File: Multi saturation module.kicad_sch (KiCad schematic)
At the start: 38 parts, among them J1 AudioJack2, J3 AudioJack2, U1 NE5532, U2 NE5532, U3 NE5532

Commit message: renamed the project
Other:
- title: Eurorack Transformer Saturation Module -> Eurorack Multi Saturation Module

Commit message: revision 0.4
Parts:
- removed C?: 1uF, symbol Device:C
- removed C?: 470uF, symbol Device:C_Polarized
- removed D?: 4148, symbol Device:D
- removed Q?: NPN, symbol Simulation_SPICE:NPN
- removed R?: 10k, symbol Device:R
- removed R? (x2): 1k5, symbol Device:R
- removed U?: VTL5C, OptoDevice:PerkinElmer_VTL5C, symbol Isolator:VTL5C
- added C1: 1uF, symbol Device:C
- added C3: 0.1uF, symbol Device:C
- added D2, D3: LED, symbol Device:LED
- added D4, D5: 4148, symbol Device:D
- added R1, R2: 10R, symbol Device:R
- added R11: 100k, symbol Device:R
- added R14, R21, R5, R9: 10k, symbol Device:R
- added R22: 6.8k, symbol Device:R
- added R3: 680R, symbol Device:R
- added R6: 330R, symbol Device:R
- added RV3: Dry_gain_10k, symbol Device:R_Potentiometer_Trim
- added SW2: Bypass_sw_DPDT, symbol Switch:SW_DPDT_x2
- added SW3: SW_SPST, symbol Switch:SW_SPST
- added U1: NE5532, symbol Amplifier_Operational:NE5532
- added U3: VTL5C, OptoDevice:PerkinElmer_VTL5C, symbol Isolator:VTL5C
- added unit 3 of U5
- RV2: renamed from RV3; value 10k -> Wet_gain_10k
- renumbered C1 to C2, R12 to R10, R9 to R13, R2 to R7, U3 to U4, U1 to U5
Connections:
- net Mix is gone; now on net Audio_out: R?.1, U?.3
- net +12V: now also U5.8 (V+)
- net -12V: now also U5.4 (V-)
- net Audio_out: no longer U?.7
- net Dry: now also U?.5 (+); no longer U2.5 (+)
- net GND: now also D4.2 (A), D5.1 (K), R11.2, R22.2, R6.2, R9.1, RV3.1, RV3.2, U3.4; no longer U?.5 (+)
- net Wet: now also C3.1, R11.1; no longer C2.1, R10.1
- net at U?.6 (-): now also R14.2, RV3.3
- net Clipping_diodes: now reaches R13.1, U4.1, U?.4
- net Clipping_diodes: now also SW3.2 (B)
- new net: C1.2, R1.1
- new net: R1.2, U1.5 (+)
- new net: R14.1, R?.2, U?.7
- new net: R2.1, U1.3 (+)
- new net: R2.2, R5.1, SW2.1 (A)
- new net: R5.2, R9.2, SW2.4 (A), U3.3
- new net: R6.1, U1.6 (-), U3.1 (-)
- new net: D2.1 (K), D3.2 (A), SW3.1 (A)
- new net: C1.1, U1.1, U1.2 (-)
- new net: C3.2, SW2.5 (B)
- new net: R21.2, SW2.2 (B), U2.7
- new net: SW2.3 (C), SW2.6 (C)
- new net: D2.2 (A), D3.1 (K), D4.1 (K), D5.2 (A)
- new net: R3.2, U1.7
- new net: R21.1, R22.1, U2.6 (-)
- new net: R3.1, U3.2 (+)
- new net: C2.1, R10.1, U2.5 (+)
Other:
- note added: "VTL5C3 R17 = 47k Silonex 32SR3 R17 = 470R Handmade Vactrol with 5mm led and LDR R17 = 47k"
- note added: "Vactrol Saturation Stage"
- note added: "dry gain compensation"
- note removed: "Output gain stage"
- note removed: "VTL5C3 R13 = 47k Silonex 32SR3 R12 = 470R Handmade Vactrol with 5mm led and LDR = 47k"
- moved on the sheet: C2, D?, J1, J?, R10, R13, R7, R?, RV2, RV?, SW?A, SW?B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

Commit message: revision 0.4 update
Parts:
- removed R9: 10k, symbol Device:R
- added C4, C5: 22uF, symbol Device:C_Polarized
- added D1: LED, symbol Device:LED
- added D7, D8: 4001, symbol Device:D
- added J4, J5: Dry_audio_out, symbol Connector_Audio:AudioJack2
- J1: value AudioJack2 -> Audio_in
- J3: value AudioJack2 -> Mix_audio_out
- renumbered C2 to C1, C1 to C2, D4 to D5, D5 to D6, R6 to R10, R5 to R12, R13 to R14, R14 to R15, R7 to R2, R2 to R4, R1 to R5, R10 to R6, R3 to R7, R21 to R8, R22 to R9, U2 to U1, U1 to U2
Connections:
- net +12V: now also C4.1, D7.1 (K)
- net -12V: now also C5.2, D8.2 (A)
- net Dry: now also J4.T
- net GND: now also C4.2, C5.1, J4.S, J5.S
- net Wet: now also J5.T
- net at R4.1: now also R12.2, SW2.1 (A); no longer U2.3 (+)
- net at SW2.4 (A), U3.3: now also R12.1; no longer R12.2
- net at R10.1, U2.6 (-), U3.1 (-): now also D1.1 (K)
- net Mix_CV_in: now reaches J?.T, R?.1, RV?.3
- net at R7.1, U3.2 (+): now also D1.2 (A)
- net Audio_out renamed Mix_audio_out
- new net: R4.2, U2.3 (+)
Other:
- moved on the sheet: C1, C2, C3, D2, D3, D5, D6, D?, J1, J3, J?, R10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

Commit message: rev 0.5 update
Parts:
- added J6: EURO_PWR_2x5, DIYSynthMNL:IDC-Header_2x05_P2.54mm_Vertical_BigPads, symbol eurocad:EURO_PWR_2x5
- added R22: 330R, DIYSynthMNL:R_quarter_watt_L6.3mm_D2.5mm_P7.62mm, symbol Device:R
- C1, C3: footprint (none) -> DIYSynthMNL:C_Rect_L7.0mm_W2.0mm_P5.00mm_BigPads
- C2: footprint (none) -> DIYSynthMNL:C_Rect_L7.0mm_W4.5mm_P5.00mm_BigPads
- C4, C5: footprint (none) -> DIYSynthMNL:CP_Radial_D4.0mm_P1.50mm
- D1, D2, D3, D?: footprint (none) -> DIYSynthMNL:LED_D5.0mm_BigPads
- D5, D6: footprint (none) -> DIYSynthMNL:D_4148_BigPads
- D7, D8: footprint (none) -> DIYSynthMNL:D_DO-41_SOD81_P7.62mm_Horizontal
- J1, J3, J4, J?: footprint (none) -> DIYSynthMNL:AudioJack_3.5mm_long_pads; symbol Connector_Audio:AudioJack2 -> benjiaomodular:PJ3001F
- J5: value Dry_audio_out -> Wet_audio_out; footprint (none) -> DIYSynthMNL:AudioJack_3.5mm_long_pads; symbol Connector_Audio:AudioJack2 -> benjiaomodular:PJ3001F
- R10, R11, R12, R14, R15, R4, R5, R6, R7, R8, R9, R? (x9): footprint (none) -> DIYSynthMNL:R_quarter_watt_L6.3mm_D2.5mm_P7.62mm
- R2: value 10k -> 100k; footprint (none) -> DIYSynthMNL:R_quarter_watt_L6.3mm_D2.5mm_P7.62mm
- RV2, RV3: footprint (none) -> DIYSynthMNL:Potentiometer_Bourns_3296W_Vertical_BigPads
- RV? (x2): footprint (none) -> DIYSynthMNL:Potentiometer_RV09_BigPads
- SW2, SW? (x2): footprint (none) -> benjiaomodular:ToggleSwitch_MTS-202_DPDT
- SW3: footprint (none) -> benjiaomodular:ToggleSwitch_MTS-102_SPDT
- T?: footprint (none) -> RF_Mini-Circuits:Mini-Circuits_CD636_H4.11mm; symbol Device:Transformer_1P_1S -> Transformer:ADTT3-2
- U1, U2, U4, U5, U? (x3): footprint (none) -> DIYSynthMNL:DIP-8_W7.62mm_LongPads
- U3, U?: footprint OptoDevice:PerkinElmer_VTL5C -> DIYSynthMNL:Handmade_vactrol_5mm
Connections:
- net Clipping_diodes: now also R22.2; no longer SW3.2 (B)
- net GND: now also T?.1, J6.3 (GND), J6.4 (GND), J6.5 (GND), J6.6 (GND), J6.7 (GND), J6.8 (GND); no longer T?.2 (AB)
- net at D8.1 (K): now also J6.10 (-12V), J6.9 (-12V)
- net at R?.2: now also T?.3; no longer T?.1 (AA)
- net at R?.2, SW?.4 (A): now also T?.6; no longer T?.3 (SA)
- net at D7.2 (A): now also J6.1 (+12V), J6.2 (+12V)
- new net: R22.1, SW3.2 (B)
- no-connect marks 0 -> 7
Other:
- moved on the sheet: R2

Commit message: Revision 5 update
This commit is before I separate the schematic parts into boards.
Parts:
- added J7: EuroPower_JST_3P, DIYSynthMNL:Eurorack_power_jst_3P, symbol DIYSynthMNL:JST_Eurorack_power_3P
- D7, D8: footprint DIYSynthMNL:D_DO-41_SOD81_P7.62mm_Horizontal -> DIYSynthMNL:D_DO-41_SOD81_P7.62mm_Horizontal_BigPads
- SW3: symbol Switch:SW_SPST -> Switch:SW_SPDT
- T?: footprint RF_Mini-Circuits:Mini-Circuits_CD636_H4.11mm -> DIYSynthMNL:Audio_transformer_TL016-R
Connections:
- net GND: now also J7.2 (GND)
- net at D7.2 (A), J6.1 (+12V), J6.2 (+12V): now also J7.1 (+12v)
- net at D8.1 (K), J6.10 (-12V), J6.9 (-12V): now also J7.3 (-12v)
- net at D2.1 (K), D3.2 (A): now also SW3.2 (B); no longer SW3.1 (A)
- net at R22.1: now also SW3.1 (A); no longer SW3.2 (B)
- no-connect marks 7 -> 8
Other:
- moved on the sheet: C4, C5, D7, D8, J6, U2C, U4C, U5C, U?C

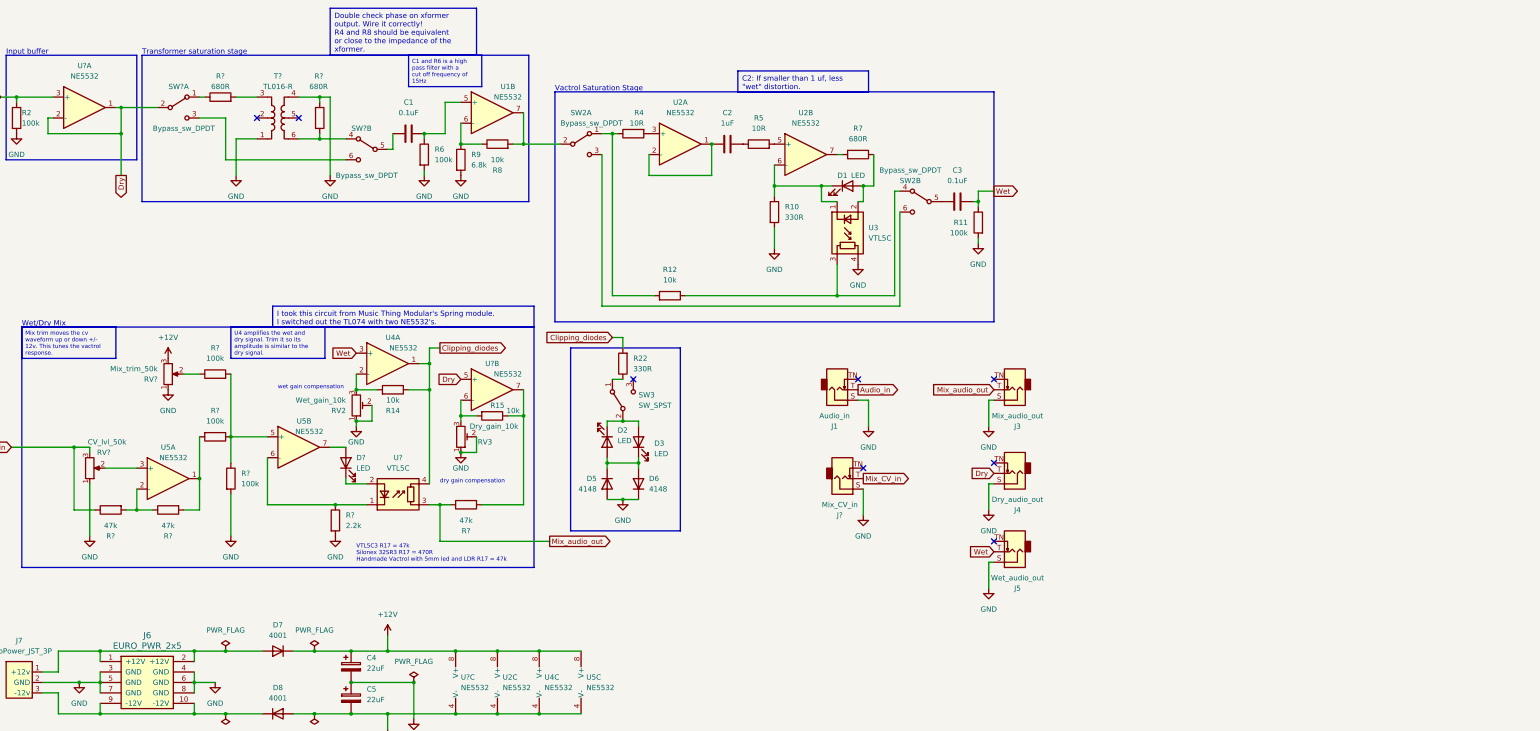
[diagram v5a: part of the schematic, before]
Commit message: Separate boards branch started
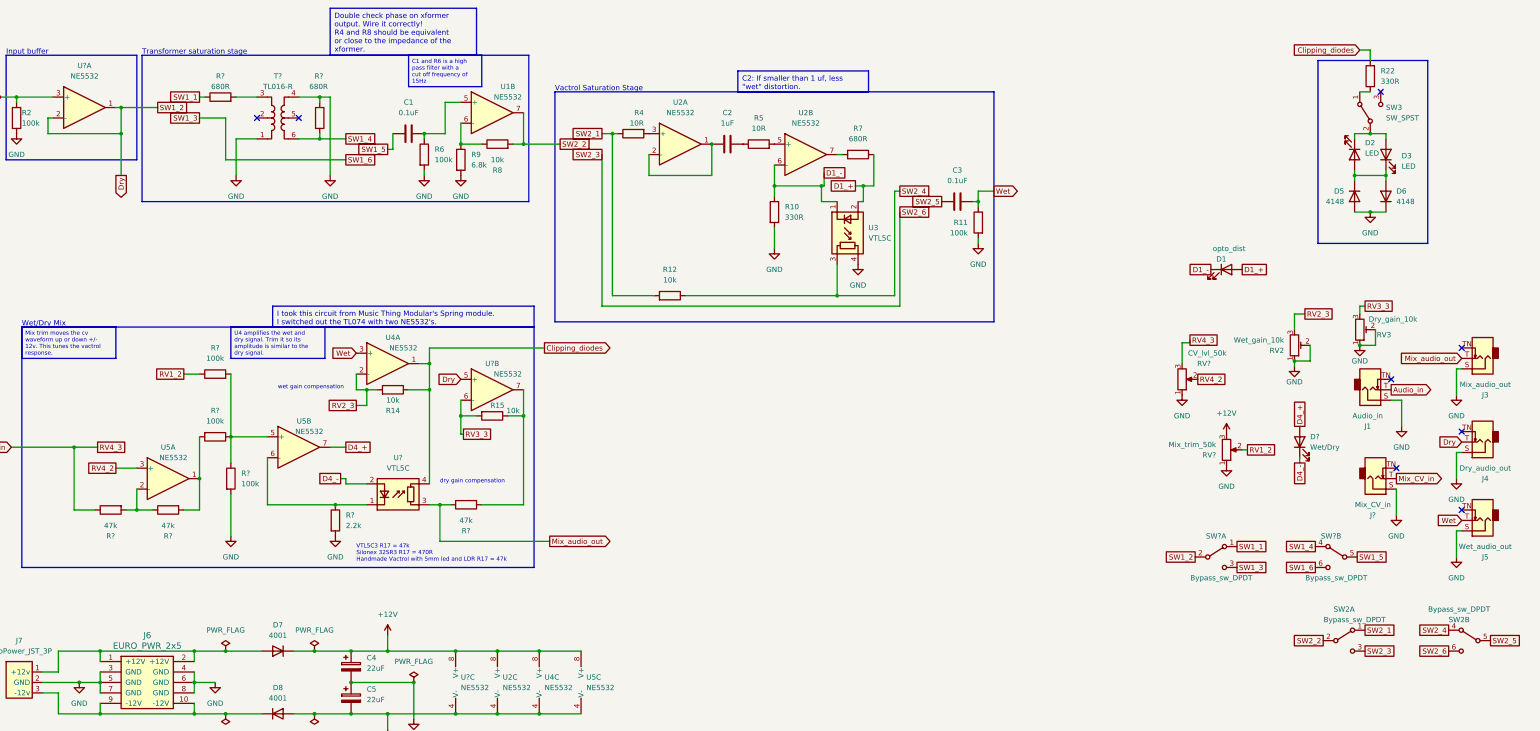
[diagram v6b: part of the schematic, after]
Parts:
- D1: value LED -> opto_dist
- D?: value LED -> Wet/Dry
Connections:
- net RV2_3: now reaches R14.2, RV2.3, U4.2 (-)
- net RV3_3: now reaches R15.2, RV3.3, U?.6 (-)
- net SW2_1: now reaches R12.2, R4.1, SW2.1 (A)
- net D4_+: now reaches D?.2 (A), U5.7
- net RV4_2: now reaches RV?.2, U5.3 (+)
- net D1_-: now reaches D1.1 (K), R10.1, U2.6 (-), U3.1 (-)
- net SW1_4: now reaches R?.2, SW?.4 (A), T?.6
- net D4_-: now reaches D?.1 (K), U?.2 (+)
- net SW2_5: now reaches C3.2, SW2.5 (B)
- net RV1_2: now reaches R?.1, RV?.2
- net SW2_2: now reaches R8.2, SW2.2 (B), U1.7
- net SW2_3: now reaches SW2.3 (C), SW2.6 (C)
- net SW2_4: now reaches R12.1, SW2.4 (A), U3.3
- net SW1_5: now reaches C1.2, SW?.5 (B)
- net SW1_3: now reaches SW?.3 (C), SW?.6 (C)
- net SW1_1: now reaches R?.1, SW?.1 (A)
- net D1_+: now reaches D1.2 (A), R7.1, U3.2 (+)
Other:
- moved on the sheet: D1, D2, D3, D5, D6, D?, J1, J3, J4, J5, J?, R22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

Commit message: Laid out footprints on three boards
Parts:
- removed C1, C3: 0.1uF, DIYSynthMNL:C_Rect_L7.0mm_W2.0mm_P5.00mm_BigPads, symbol Device:C
- removed C2: 1uF, DIYSynthMNL:C_Rect_L7.0mm_W4.5mm_P5.00mm_BigPads, symbol Device:C
- removed C4, C5: 22uF, DIYSynthMNL:CP_Radial_D4.0mm_P1.50mm, symbol Device:C_Polarized
- removed D1: opto_dist, DIYSynthMNL:LED_D5.0mm_BigPads, symbol Device:LED
- removed D2, D3: LED, DIYSynthMNL:LED_D5.0mm_BigPads, symbol Device:LED
- removed D5, D6: 4148, DIYSynthMNL:D_4148_BigPads, symbol Device:D
- removed D7, D8: 4001, DIYSynthMNL:D_DO-41_SOD81_P7.62mm_Horizontal_BigPads, symbol Device:D
- removed D?: Wet/Dry, DIYSynthMNL:LED_D5.0mm_BigPads, symbol Device:LED
- removed J1: Audio_in, DIYSynthMNL:AudioJack_3.5mm_long_pads, symbol benjiaomodular:PJ3001F
- removed J3: Mix_audio_out, DIYSynthMNL:AudioJack_3.5mm_long_pads, symbol benjiaomodular:PJ3001F
- removed J4: Dry_audio_out, DIYSynthMNL:AudioJack_3.5mm_long_pads, symbol benjiaomodular:PJ3001F
- removed J5: Wet_audio_out, DIYSynthMNL:AudioJack_3.5mm_long_pads, symbol benjiaomodular:PJ3001F
- removed J6: EURO_PWR_2x5, DIYSynthMNL:IDC-Header_2x05_P2.54mm_Vertical_BigPads, symbol eurocad:EURO_PWR_2x5
- removed J7: EuroPower_JST_3P, DIYSynthMNL:Eurorack_power_jst_3P, symbol DIYSynthMNL:JST_Eurorack_power_3P
- removed J?: Mix_CV_in, DIYSynthMNL:AudioJack_3.5mm_long_pads, symbol benjiaomodular:PJ3001F
- removed R10, R22: 330R, DIYSynthMNL:R_quarter_watt_L6.3mm_D2.5mm_P7.62mm, symbol Device:R
- removed R11, R2, R6, R? (x3): 100k, DIYSynthMNL:R_quarter_watt_L6.3mm_D2.5mm_P7.62mm, symbol Device:R
- removed R12, R14, R15, R8: 10k, DIYSynthMNL:R_quarter_watt_L6.3mm_D2.5mm_P7.62mm, symbol Device:R
- removed R4, R5: 10R, DIYSynthMNL:R_quarter_watt_L6.3mm_D2.5mm_P7.62mm, symbol Device:R
- removed R7, R? (x2): 680R, DIYSynthMNL:R_quarter_watt_L6.3mm_D2.5mm_P7.62mm, symbol Device:R
- removed R9: 6.8k, DIYSynthMNL:R_quarter_watt_L6.3mm_D2.5mm_P7.62mm, symbol Device:R
- removed R? (x3): 47k, DIYSynthMNL:R_quarter_watt_L6.3mm_D2.5mm_P7.62mm, symbol Device:R
- removed R?: 2.2k, DIYSynthMNL:R_quarter_watt_L6.3mm_D2.5mm_P7.62mm, symbol Device:R
- removed RV2: Wet_gain_10k, DIYSynthMNL:Potentiometer_Bourns_3296W_Vertical_BigPads, symbol Device:R_Potentiometer_Trim
- removed RV3: Dry_gain_10k, DIYSynthMNL:Potentiometer_Bourns_3296W_Vertical_BigPads, symbol Device:R_Potentiometer_Trim
- removed RV?: CV_lvl_50k, DIYSynthMNL:Potentiometer_RV09_BigPads, symbol Device:R_Potentiometer
- removed RV?: Mix_trim_50k, DIYSynthMNL:Potentiometer_RV09_BigPads, symbol Device:R_Potentiometer
- removed SW2, SW? (x2): Bypass_sw_DPDT, benjiaomodular:ToggleSwitch_MTS-202_DPDT, symbol Switch:SW_DPDT_x2
- removed SW3: SW_SPST, benjiaomodular:ToggleSwitch_MTS-102_SPDT, symbol Switch:SW_SPDT
- removed T?: TL016-R, DIYSynthMNL:Audio_transformer_TL016-R, symbol Transformer:ADTT3-2
- removed U1, U2, U4, U5, U? (x3): NE5532, DIYSynthMNL:DIP-8_W7.62mm_LongPads, symbol Amplifier_Operational:NE5532
- removed U3, U?: VTL5C, DIYSynthMNL:Handmade_vactrol_5mm, symbol Isolator:VTL5C
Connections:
- no-connect marks 8 -> 0
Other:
- added sheet Board_A (Multi_Saturation_Board_A.kicad_sch)
- added sheet Board_B (Multi_Saturation_Board_B.kicad_sch)
- note removed: "Input buffer"
- note removed: "Transformer saturation stage"
- note removed: "VTL5C3 R17 = 47k Silonex 32SR3 R17 = 470R Handmade Vactrol with 5mm led and LDR R17 = 47k"
- note removed: "Vactrol Saturation Stage"
- note removed: "Wet/Dry Mix"
- note removed: "dry gain compensation"
- note removed: "wet gain compensation"

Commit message: cleaned up project directory
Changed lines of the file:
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@@
   (title_block
     (title "Eurorack Multi Saturation Module")
-    (date "2023-12-24")
-    (rev "0.5")
+    (date "2023-12-28")
+    (rev "0.6")
     (company "DIYSynthManila")
     (comment 1 "This version is a prototype.")
   )
-  (sheet (at 240.665 22.225) (size 23.495 5.08) (fields_autoplaced)
+  (sheet (at 131.445 89.535) (size 23.495 5.08) (fields_autoplaced)
     (stroke (width 0.1524) (type solid))
     (fill (color 0 0 0 0.0000))
-    (property "Sheetname" "Board_A" (at 240.665 21.5134 0)
+    (property "Sheetname" "Board_A" (at 131.445 88.8234 0)
       (effects (font (size 1.27 1.27)) (justify left bottom))
     )
-    (property "Sheetfile" "Multi_Saturation_Board_A.kicad_sch" (at 240.665 27.8896 0)
+    (property "Sheetfile" "Multi_Saturation_Board_A.kicad_sch" (at 131.445 95.1996 0)
       (effects (font (size 1.27 1.27)) (justify left top))
     )
@@
     )
   )
-  (sheet (at 240.665 32.385) (size 23.495 4.445) (fields_autoplaced)
+  (sheet (at 131.445 99.695) (size 23.495 4.445) (fields_autoplaced)
     (stroke (width 0.1524) (type solid))
     (fill (color 0 0 0 0.0000))
-    (property "Sheetname" "Board_B" (at 240.665 31.6734 0)
+    (property "Sheetname" "Board_B" (at 131.445 98.9834 0)
       (effects (font (size 1.27 1.27)) (justify left bottom))
     )
-    (property "Sheetfile" "Multi_Saturation_Board_B.kicad_sch" (at 240.665 37.4146 0)
+    (property "Sheetfile" "Multi_Saturation_Board_B.kicad_sch" (at 131.445 104.7246 0)
       (effects (font (size 1.27 1.27)) (justify left top))
     )
